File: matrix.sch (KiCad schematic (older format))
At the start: 134 parts, among them SW1 ESC, SW10 #9, SW11 #0, SW12 -_, SW13 =+, SW14 BSPC, SW15 INSR, SW16 TAB, SW17 Q, SW18 W, SW19 E, SW2 #1, SW20 R, SW21 T, SW22 Y, SW23 U, SW24 I, SW25 O, SW26 P, SW27 [{, SW28 ]}, SW29 \\|, SW3 #2, SW30 DLTE, SW31 CAPS, SW32 A, SW33 S, SW34 D, SW35 F, SW36 G, SW37 H, SW38 J, SW39 K, SW4 #3, SW40 L, SW41 ;:, SW42 '\", SW43 ENTR, SW44 PGUP, SW45 LSHF, SW46 Z, SW47 X, SW48 C, SW49 V, SW5 #4, SW50 B, SW51 N, SW52 M, SW53 ,<, SW54 .>, SW55 /?, SW56 RSHF, SW57 UARW, SW58 PGDN, SW59 LCTR, SW6 #5, SW60 WNDW, SW61 LALT, SW62 SPCB, SW63 RALT, SW64 FNKY, SW65 LARW, SW66 DARW, SW67 RARW, SW7 #6, SW8 #7, SW9 #8

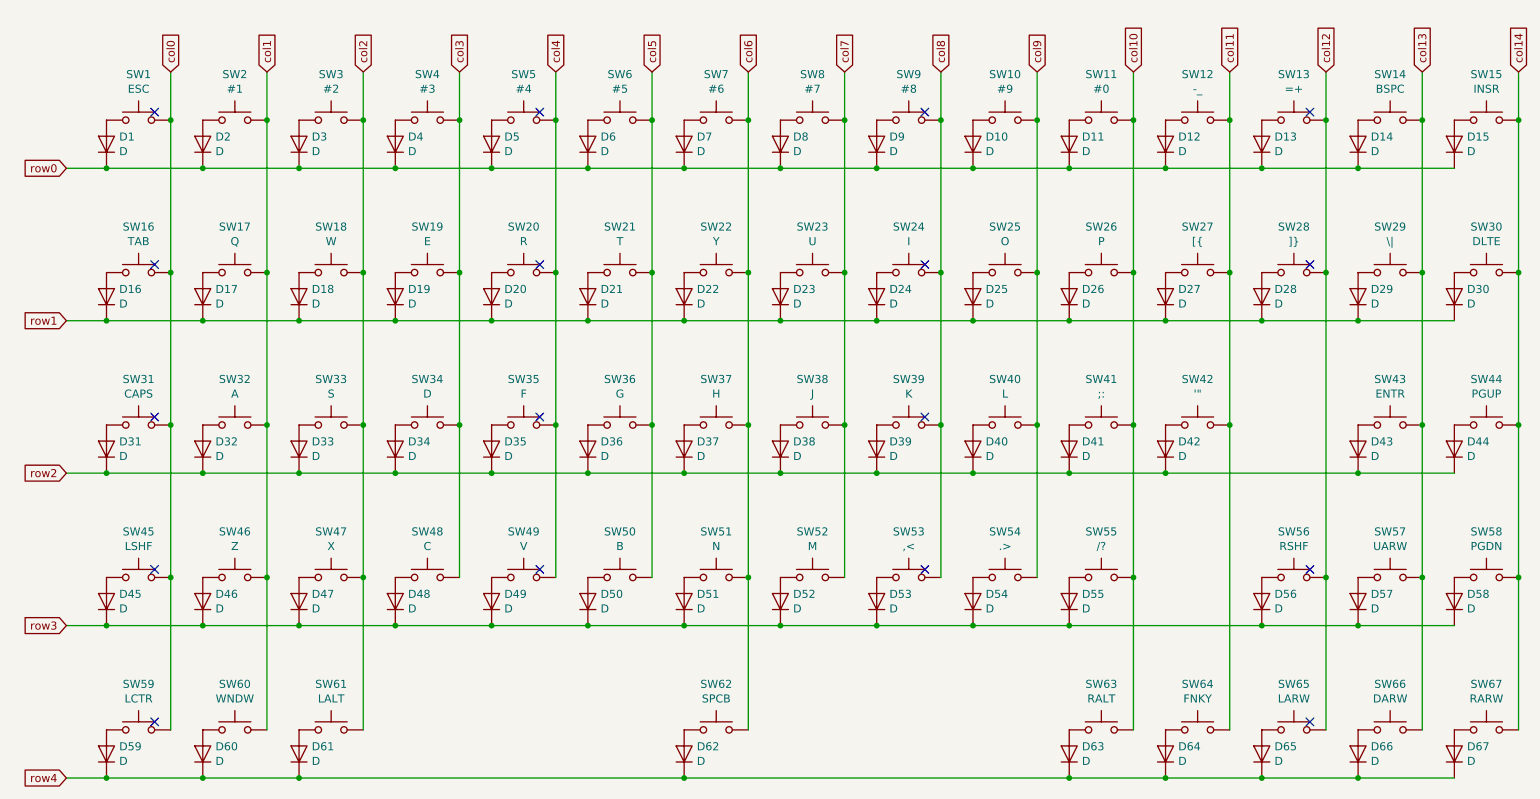
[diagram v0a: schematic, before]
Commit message: flipped switches
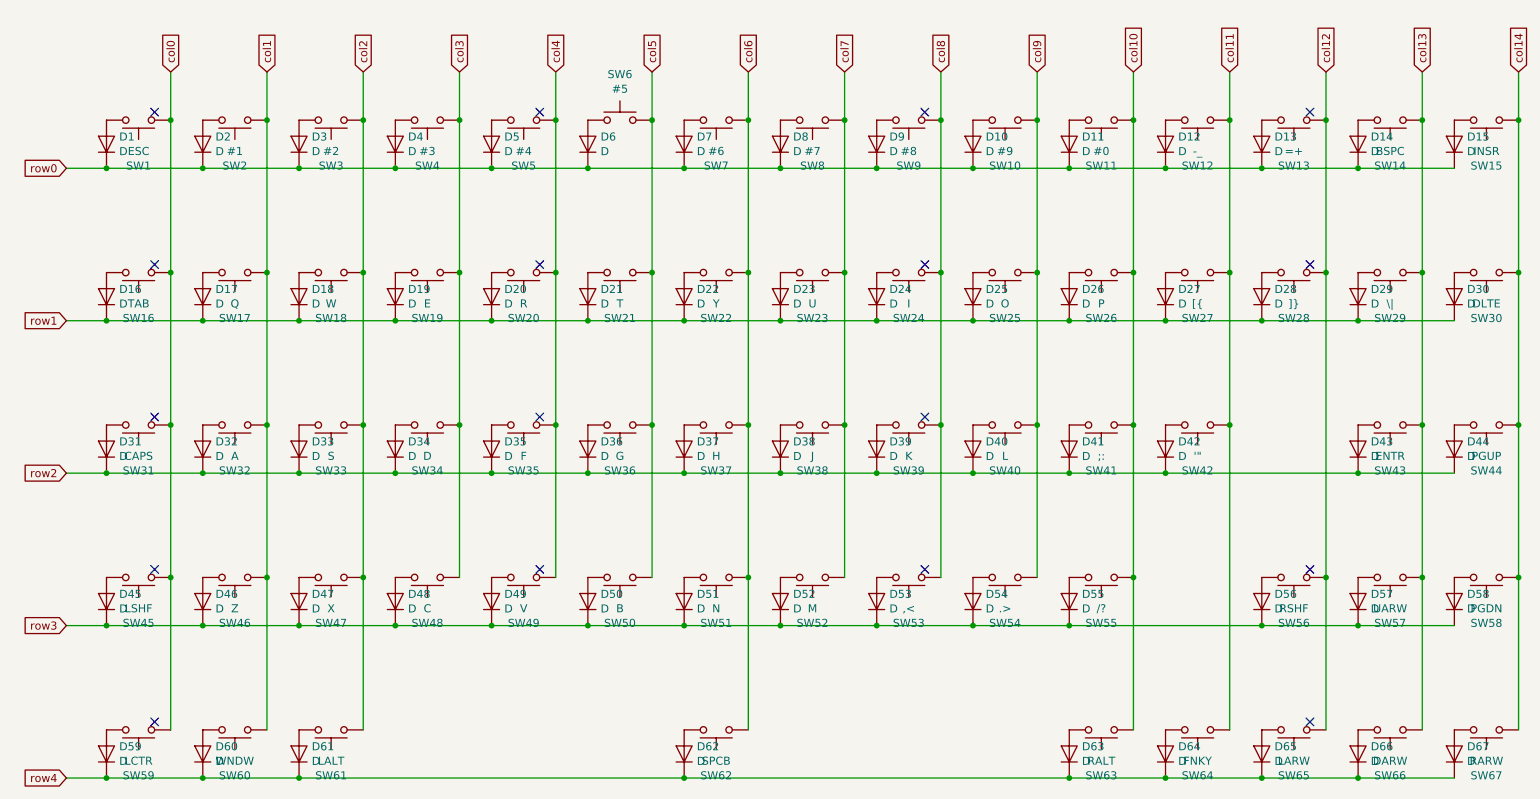
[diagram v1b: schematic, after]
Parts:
- SW14: footprint MX_Only:MXOnly-1U-NoLED -> MX_Only:MXOnly-2U-NoLED
- SW29: footprint MX_Only:MXOnly-1U-NoLED -> MX_Only:MXOnly-1.5U-NoLED
- SW43: footprint MX_Only:MXOnly-1U-NoLED -> MX_Only:MXOnly-2.25U-NoLED
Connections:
- net col0: now also SW1.1, SW16.1, SW31.1, SW45.1, SW59.1; no longer SW1.2, SW16.2, SW31.2, SW45.2, SW59.2
- net col1: now also SW17.1, SW2.1, SW32.1, SW46.1, SW60.1; no longer SW17.2, SW2.2, SW32.2, SW46.2, SW60.2
- net col10: now also SW11.1, SW26.1, SW41.1, SW55.1, SW63.1; no longer SW11.2, SW26.2, SW41.2, SW55.2, SW63.2
- net col11: now also SW12.1, SW27.1, SW42.1, SW64.1; no longer SW12.2, SW27.2, SW42.2, SW64.2
- net col12: now also SW13.1, SW28.1, SW56.1, SW65.1; no longer SW13.2, SW28.2, SW56.2, SW65.2
- net col13: now also SW14.1, SW29.1, SW43.1, SW57.1, SW66.1; no longer SW14.2, SW29.2, SW43.2, SW57.2, SW66.2
- net col14: now also SW15.1, SW30.1, SW44.1, SW58.1, SW67.1; no longer SW15.2, SW30.2, SW44.2, SW58.2, SW67.2
- net col2: now also SW18.1, SW3.1, SW33.1, SW47.1, SW61.1; no longer SW18.2, SW3.2, SW33.2, SW47.2, SW61.2
- net col3: now also SW19.1, SW34.1, SW4.1, SW48.1; no longer SW19.2, SW34.2, SW4.2, SW48.2
- net col4: now also SW20.1, SW35.1, SW49.1, SW5.1; no longer SW20.2, SW35.2, SW49.2, SW5.2
- net col5: now also SW21.1, SW36.1, SW50.1; no longer SW21.2, SW36.2, SW50.2
- net col6: now also SW22.1, SW37.1, SW51.1, SW62.1, SW7.1; no longer SW22.2, SW37.2, SW51.2, SW62.2, SW7.2
- net col7: now also SW23.1, SW38.1, SW52.1, SW8.1; no longer SW23.2, SW38.2, SW52.2, SW8.2
- net col8: now also SW24.1, SW39.1, SW53.1, SW9.1; no longer SW24.2, SW39.2, SW53.2, SW9.2
- net col9: now also SW10.1, SW25.1, SW40.1, SW54.1; no longer SW10.2, SW25.2, SW40.2, SW54.2
- net at D1.2 (A): now also SW1.2; no longer SW1.1
- net at D2.2 (A): now also SW2.2; no longer SW2.1
- net at D3.2 (A): now also SW3.2; no longer SW3.1
- net at D4.2 (A): now also SW4.2; no longer SW4.1
- net at D5.2 (A): now also SW5.2; no longer SW5.1
- net at D7.2 (A): now also SW7.2; no longer SW7.1
- net at D8.2 (A): now also SW8.2; no longer SW8.1
- net at D9.2 (A): now also SW9.2; no longer SW9.1
- net at D10.2 (A): now also SW10.2; no longer SW10.1
- net at D11.2 (A): now also SW11.2; no longer SW11.1
- net at D12.2 (A): now also SW12.2; no longer SW12.1
- net at D13.2 (A): now also SW13.2; no longer SW13.1
- net at D14.2 (A): now also SW14.2; no longer SW14.1
- net at D15.2 (A): now also SW15.2; no longer SW15.1
- net at D16.2 (A): now also SW16.2; no longer SW16.1
- net at D17.2 (A): now also SW17.2; no longer SW17.1
- net at D18.2 (A): now also SW18.2; no longer SW18.1
- net at D19.2 (A): now also SW19.2; no longer SW19.1
- net at D20.2 (A): now also SW20.2; no longer SW20.1
- net at D21.2 (A): now also SW21.2; no longer SW21.1
- net at D22.2 (A): now also SW22.2; no longer SW22.1
- net at D23.2 (A): now also SW23.2; no longer SW23.1
- net at D24.2 (A): now also SW24.2; no longer SW24.1
- net at D25.2 (A): now also SW25.2; no longer SW25.1
- net at D26.2 (A): now also SW26.2; no longer SW26.1
- net at D27.2 (A): now also SW27.2; no longer SW27.1
- net at D28.2 (A): now also SW28.2; no longer SW28.1
- net at D29.2 (A): now also SW29.2; no longer SW29.1
- net at D30.2 (A): now also SW30.2; no longer SW30.1
- net at D31.2 (A): now also SW31.2; no longer SW31.1
- net at D32.2 (A): now also SW32.2; no longer SW32.1
- net at D33.2 (A): now also SW33.2; no longer SW33.1
- net at D34.2 (A): now also SW34.2; no longer SW34.1
- net at D35.2 (A): now also SW35.2; no longer SW35.1
- net at D36.2 (A): now also SW36.2; no longer SW36.1
- net at D37.2 (A): now also SW37.2; no longer SW37.1
- net at D38.2 (A): now also SW38.2; no longer SW38.1
- net at D39.2 (A): now also SW39.2; no longer SW39.1
- net at D40.2 (A): now also SW40.2; no longer SW40.1
- net at D41.2 (A): now also SW41.2; no longer SW41.1
- net at D42.2 (A): now also SW42.2; no longer SW42.1
- net at D43.2 (A): now also SW43.2; no longer SW43.1
- net at D44.2 (A): now also SW44.2; no longer SW44.1
- net at D45.2 (A): now also SW45.2; no longer SW45.1
- net at D46.2 (A): now also SW46.2; no longer SW46.1
- net at D47.2 (A): now also SW47.2; no longer SW47.1
- net at D48.2 (A): now also SW48.2; no longer SW48.1
- net at D49.2 (A): now also SW49.2; no longer SW49.1
- net at D50.2 (A): now also SW50.2; no longer SW50.1
- net at D51.2 (A): now also SW51.2; no longer SW51.1
- net at D52.2 (A): now also SW52.2; no longer SW52.1
- net at D53.2 (A): now also SW53.2; no longer SW53.1
- net at D54.2 (A): now also SW54.2; no longer SW54.1
- net at D55.2 (A): now also SW55.2; no longer SW55.1
- net at D56.2 (A): now also SW56.2; no longer SW56.1
- net at D57.2 (A): now also SW57.2; no longer SW57.1
- net at D58.2 (A): now also SW58.2; no longer SW58.1
- net at D59.2 (A): now also SW59.2; no longer SW59.1
- net at D60.2 (A): now also SW60.2; no longer SW60.1
- net at D61.2 (A): now also SW61.2; no longer SW61.1
- net at D62.2 (A): now also SW62.2; no longer SW62.1
- net at D63.2 (A): now also SW63.2; no longer SW63.1
- net at D64.2 (A): now also SW64.2; no longer SW64.1
- net at D65.2 (A): now also SW65.2; no longer SW65.1
- net at D66.2 (A): now also SW66.2; no longer SW66.1
- net at D67.2 (A): now also SW67.2; no longer SW67.1
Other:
- moved on the sheet: SW1, SW10, SW11, SW12, SW13, SW14, SW15, SW16, SW17, SW18, SW19, SW2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

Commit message: more pcb
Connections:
- net col5: now also SW6.1; no longer SW6.2
- net at D6.2 (A): now also SW6.2; no longer SW6.1
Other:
- moved on the sheet: SW6
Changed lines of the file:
@@
 F 3 "~" H 4350 1400 50  0001 C CNN
 	1    4350 1200
-	1    0    0    -1
+	-1   0    0    1
 $EndComp
 $Comp
@@
 $EndComp
 NoConn ~ 8650 1150
-Wire Wire Line
-	4550 1200 4550 900
 Text GLabel 1550 900  1    50   Input ~ 0
 col0
@@
 	-1   0    0    1
 $EndComp
-Connection ~ 4550 1200
 $Comp
 L Device:D D31
@@
 	6350 1200 6350 2150
 Connection ~ 6350 2150
-Wire Wire Line
-	4550 1200 4550 2150
 Connection ~ 4550 2150
 Wire Wire Line
@@
 Wire Wire Line
 	1550 4050 1550 5000
+Wire Wire Line
+	4550 900  4550 1200
+Connection ~ 4550 1200
+Wire Wire Line
+	4550 1200 4550 2150
 $EndSCHEMATC
